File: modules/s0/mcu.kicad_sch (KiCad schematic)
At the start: 8 parts, among them SW1 SW_Push, U6 ESP32-C3-MINI-1U-H4

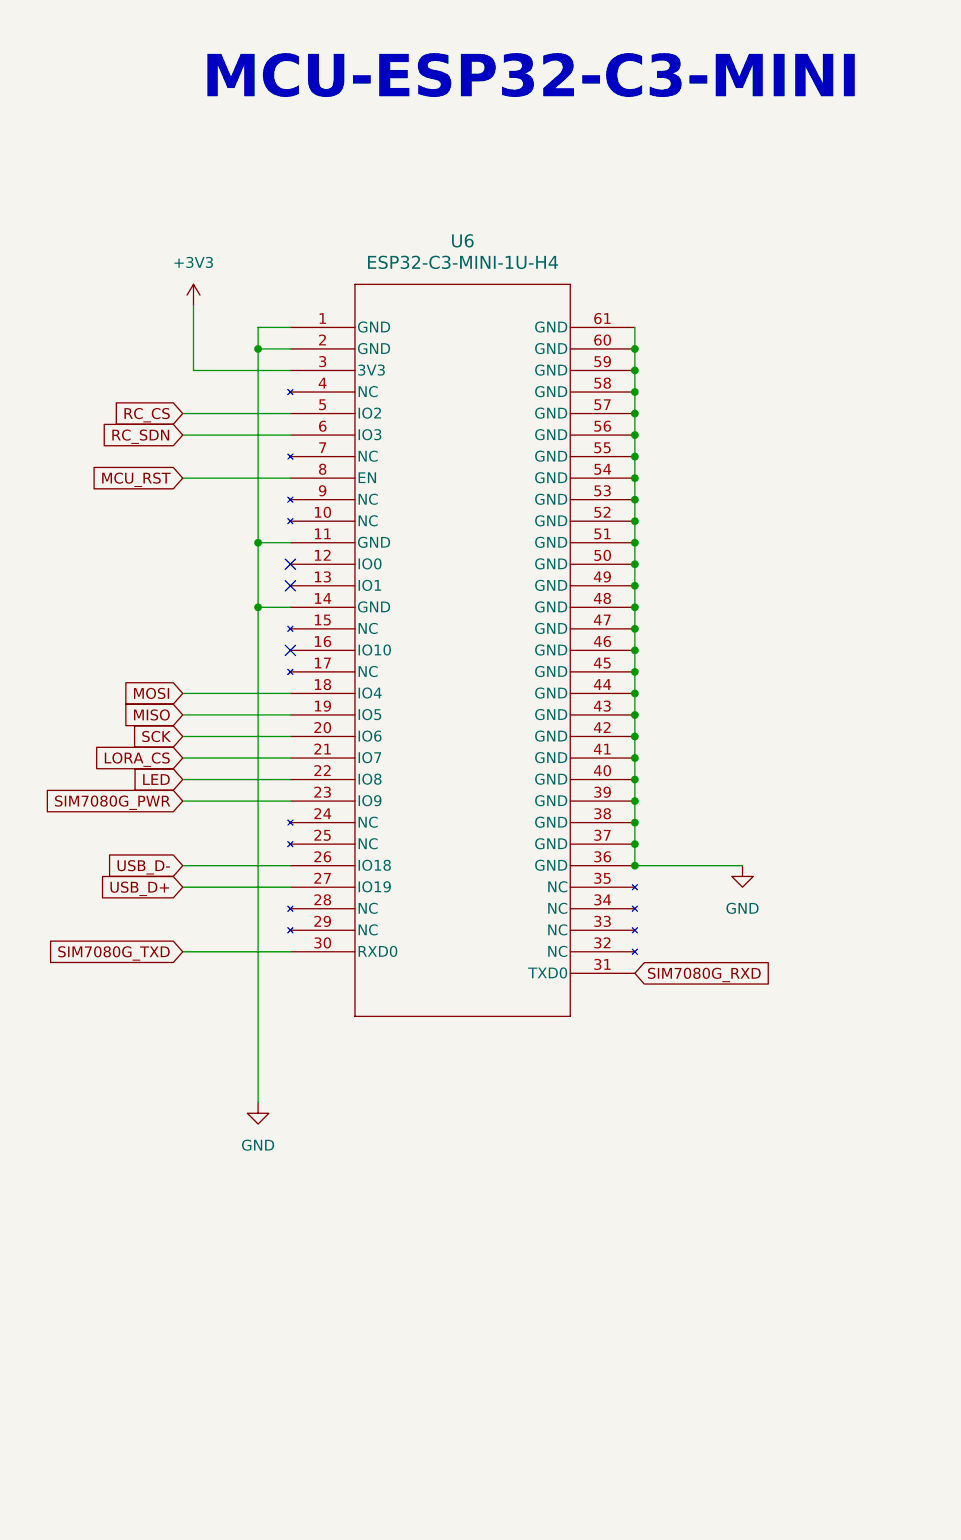
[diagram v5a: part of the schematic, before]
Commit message: feat(s0): add GPIO mux for wired mbus and sd card
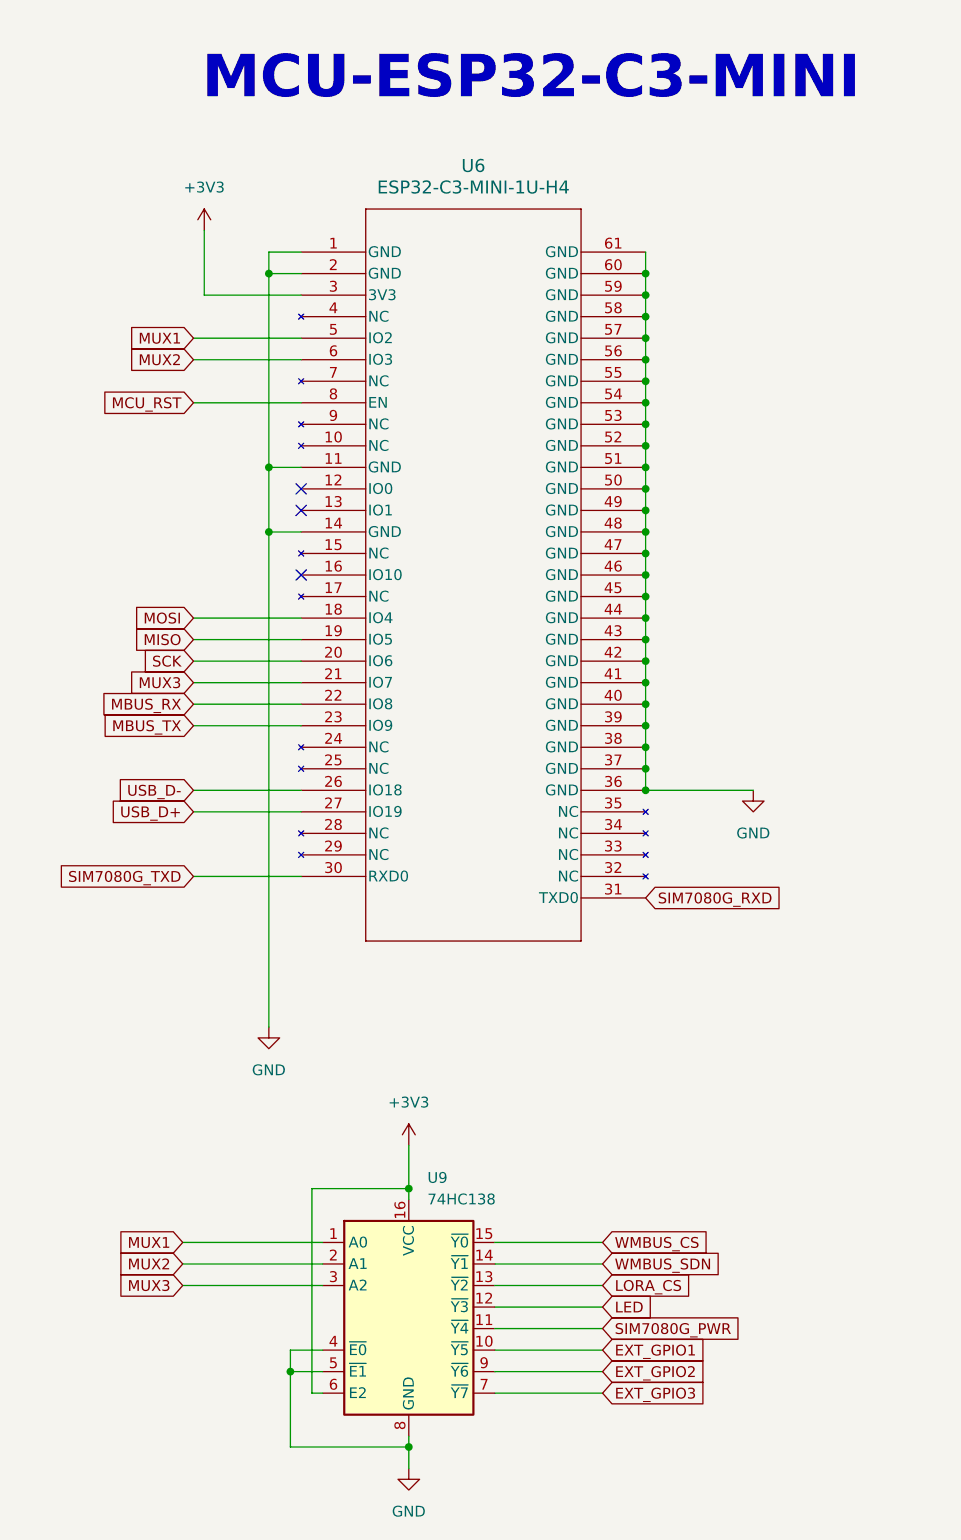
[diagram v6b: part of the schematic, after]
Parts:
- added U9: 74HC138, Package_SO:SOIC-16_3.9x9.9mm_P1.27mm, symbol 74xx:74HC138
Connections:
- net +3V3: now also U9.16 (VCC), U9.6 (E2)
- net GND: now also U9.4 (~{E0}), U9.5 (~{E1}), U9.8 (GND)
- net LED: now also U9.12 (~{Y3}); no longer U6.22 (IO8)
- net LORA_CS: now also U9.13 (~{Y2}); no longer U6.21 (IO7)
- net SIM7080G_PWR: now also U9.11 (~{Y4}); no longer U6.23 (IO9)
- net RC_CS renamed MUX1
- net MUX1: now also U9.1 (A0)
- net RC_SDN renamed MUX2
- net MUX2: now also U9.2 (A1)
- new net EXT_GPIO1: U9.10 (~{Y5})
- new net EXT_GPIO2: U9.9 (~{Y6})
- new net EXT_GPIO3: U9.7 (~{Y7})
- new net MBUS_RX: U6.22 (IO8)
- new net MBUS_TX: U6.23 (IO9)
- new net MUX3: U6.21 (IO7), U9.3 (A2)
- new net WMBUS_CS: U9.15 (~{Y0})
- new net WMBUS_SDN: U9.14 (~{Y1})
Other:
- moved on the sheet: U6

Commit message: fix: route PCB
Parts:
- U9: JLCPCB (none) -> C6818
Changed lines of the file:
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@@
+			)
+		)
+		(property "JLCPCB" "C6818"
+			(at 72.39 171.45 0)
+			(effects
+				(font
+					(size 1.27 1.27)
+				)
+				(hide yes)
 			)
 		)

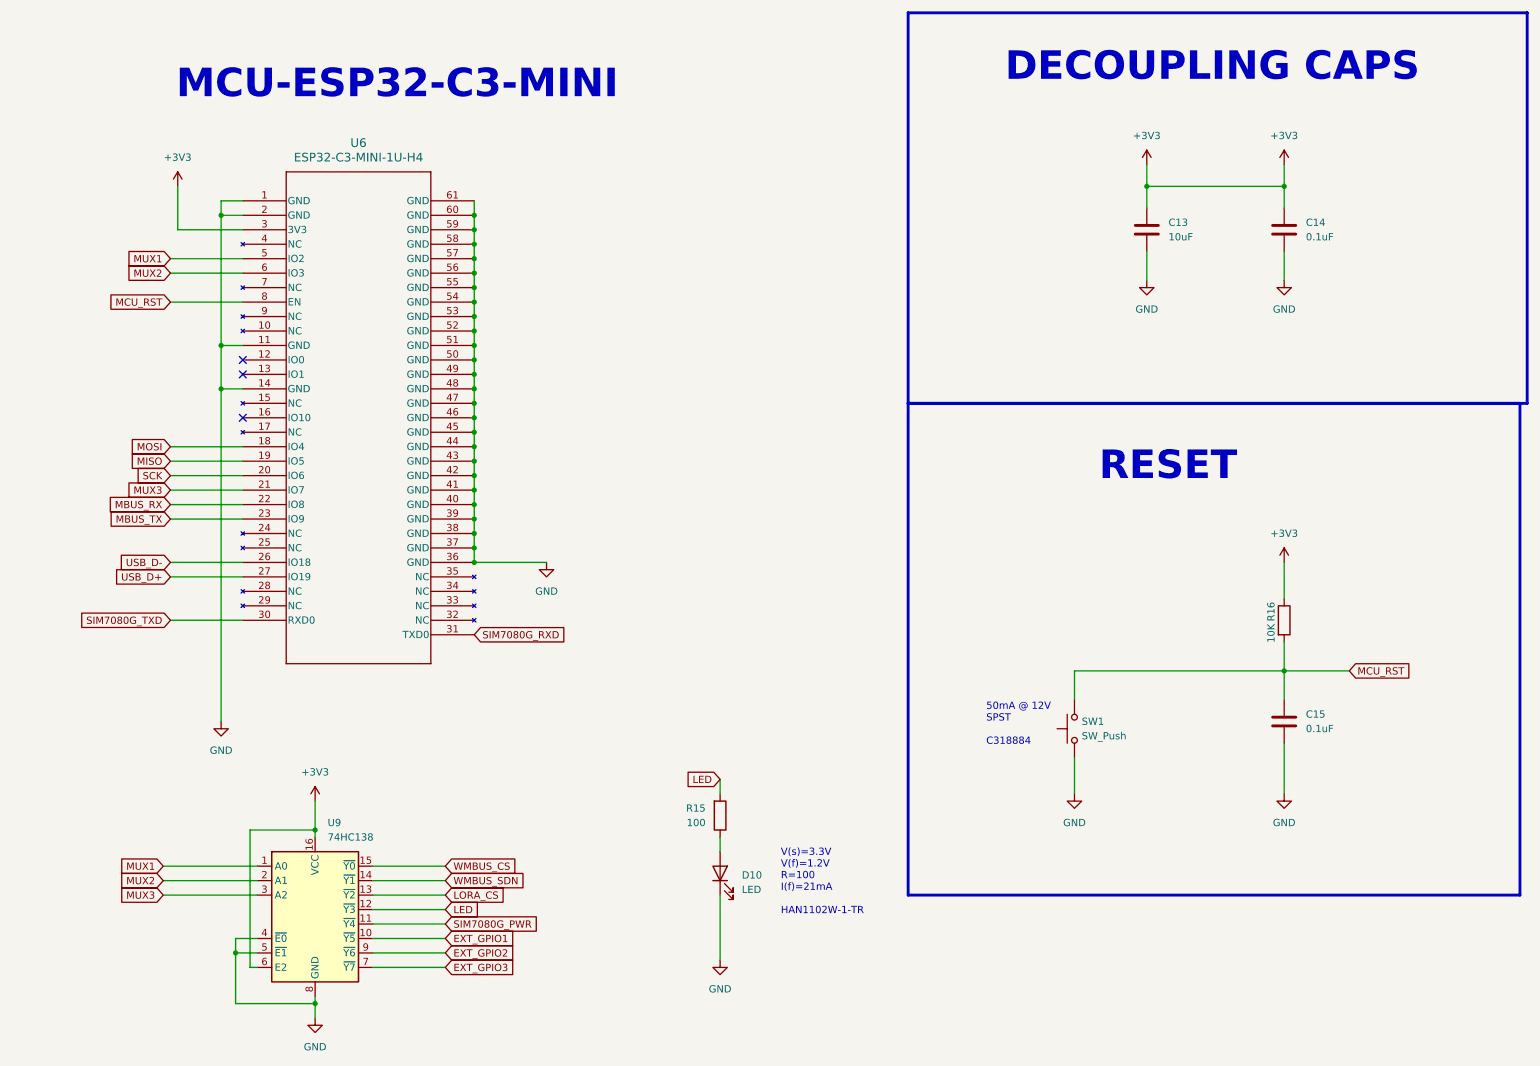
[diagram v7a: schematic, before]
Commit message: feat(s0): migrate from c3 to c6
Signed-off-by: Rodney Osodo <socials@rodneyosodo.com>
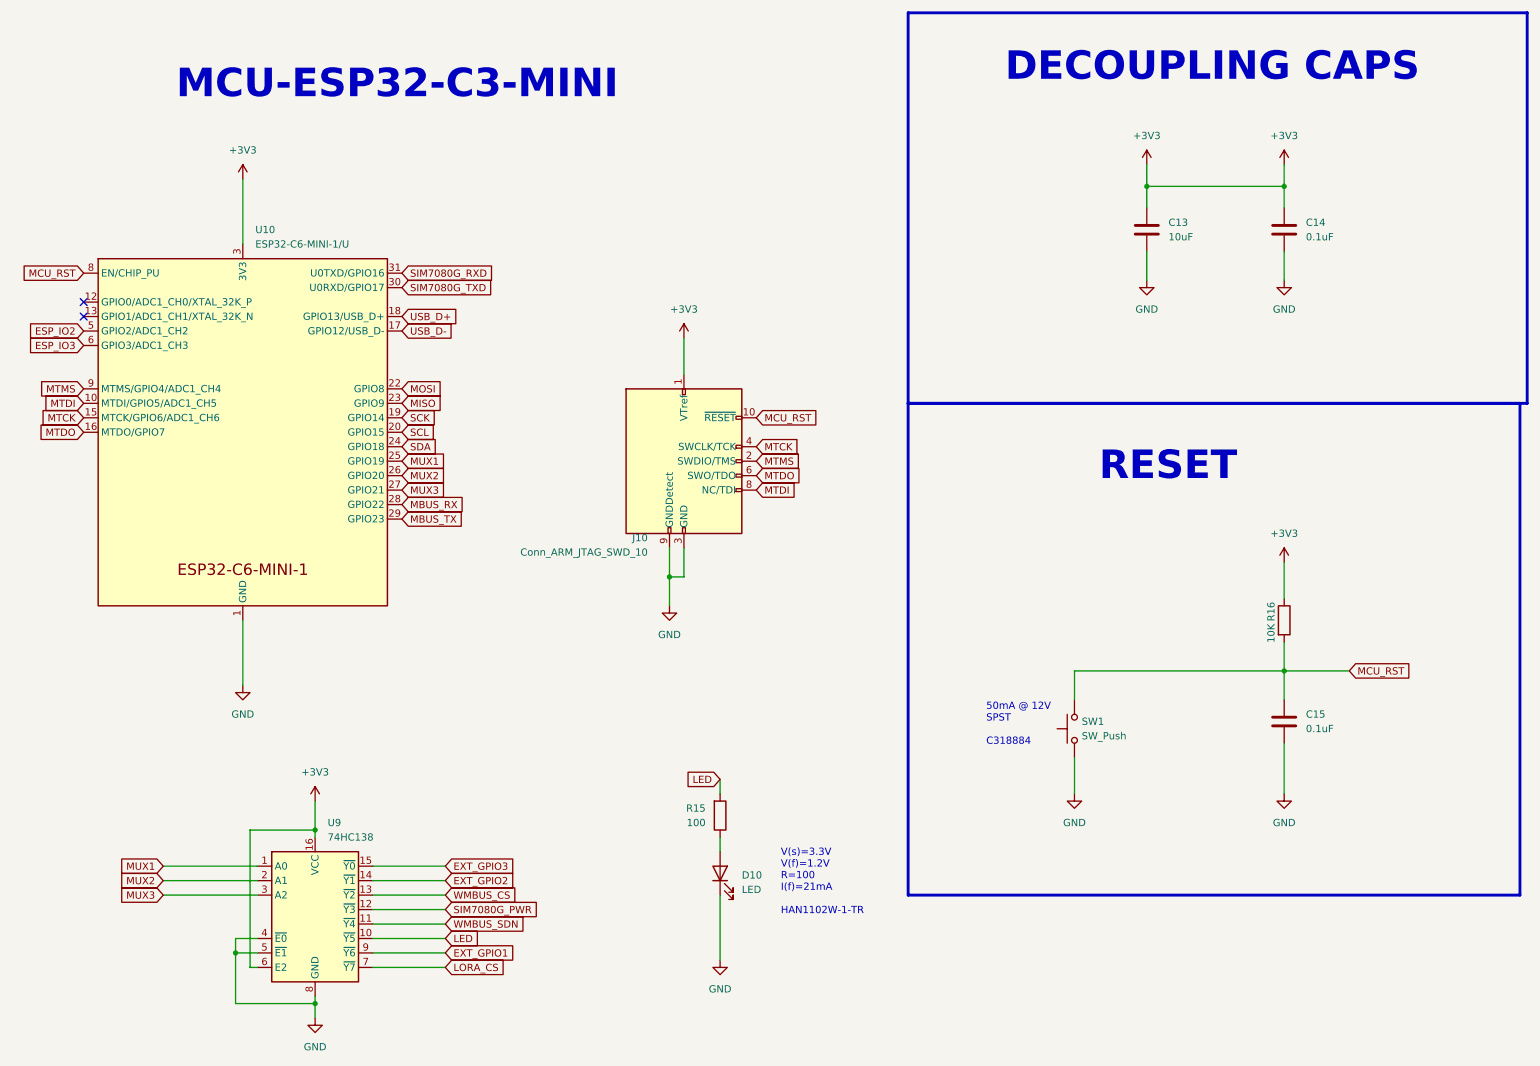
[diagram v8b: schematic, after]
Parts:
- removed U6: ESP32-C3-MINI-1U-H4, modules:XCVR_ESP32-C3-MINI-1U-N4, symbol 2024-11-20_06-36-54:ESP32-C3-MINI-1U-H4
- added J10: Conn_ARM_JTAG_SWD_10, Connector_PinHeader_1.27mm:PinHeader_2x05_P1.27mm_Vertical, symbol Connector:Conn_ARM_JTAG_SWD_10
- added U10: ESP32-C6-MINI-1/U, PCM_Espressif:ESP32-C6-MINI-1U, symbol PCM_Espressif:ESP32-C6-MINI-1/U
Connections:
- net +3V3: now also J10.1 (VTref), U10.3 (3V3)
- net EXT_GPIO1: now also U9.9 (~{Y6}); no longer U9.10 (~{Y5})
- net EXT_GPIO2: now also U9.14 (~{Y1}); no longer U9.9 (~{Y6})
- net EXT_GPIO3: now also U9.15 (~{Y0}); no longer U9.7 (~{Y7})
- net GND: now also J10.3 (GND), J10.5 (GND), J10.9 (GNDDetect), U10.1 (GND), U10.11 (GND), U10.14 (GND), U10.2 (GND), U10.36 (GND), U10.37 (GND), U10.38 (GND), U10.39 (GND), U10.40 (GND), U10.41 (GND), U10.42 (GND), U10.43 (GND), U10.44 (GND), U10.45 (GND), U10.46 (GND), U10.47 (GND), U10.48 (GND), U10.49 (GND), U10.50 (GND), U10.51 (GND), U10.52 (GND), U10.53 (GND)
- net LED: now also U9.10 (~{Y5}); no longer U9.12 (~{Y3})
- net LORA_CS: now also U9.7 (~{Y7}); no longer U9.13 (~{Y2})
- net MBUS_RX: now also U10.28 (GPIO22)
- net MBUS_TX: now also U10.29 (GPIO23)
- net MCU_RST: now also J10.10 (~{RESET}), U10.8 (EN/CHIP_PU)
- net MISO: now also U10.23 (GPIO9)
- net MOSI: now also U10.22 (GPIO8)
- net MUX1: now also U10.25 (GPIO19)
- net MUX2: now also U10.26 (GPIO20)
- net MUX3: now also U10.27 (GPIO21)
- net SCK: now also U10.19 (GPIO14)
- net SIM7080G_PWR: now also U9.12 (~{Y3}); no longer U9.11 (~{Y4})
- net SIM7080G_RXD: now also U10.31 (U0TXD/GPIO16)
- net SIM7080G_TXD: now also U10.30 (U0RXD/GPIO17)
- net USB_D+: now also U10.18 (GPIO13/USB_D+)
- net USB_D-: now also U10.17 (GPIO12/USB_D-)
- net WMBUS_CS: now also U9.13 (~{Y2}); no longer U9.15 (~{Y0})
- net WMBUS_SDN: now also U9.11 (~{Y4}); no longer U9.14 (~{Y1})
- new net ESP_IO2: U10.5 (GPIO2/ADC1_CH2)
- new net ESP_IO3: U10.6 (GPIO3/ADC1_CH3)
- new net MTCK: J10.4 (SWCLK/TCK), U10.15 (MTCK/GPIO6/ADC1_CH6)
- new net MTDI: J10.8 (NC/TDI), U10.10 (MTDI/GPIO5/ADC1_CH5)
- new net MTDO: J10.6 (SWO/TDO), U10.16 (MTDO/GPIO7)
- new net MTMS: J10.2 (SWDIO/TMS), U10.9 (MTMS/GPIO4/ADC1_CH4)
- new net SCL: U10.20 (GPIO15)
- new net SDA: U10.24 (GPIO18)
- no-connect marks 3 -> 2
